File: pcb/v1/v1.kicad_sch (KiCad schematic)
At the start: 0 parts

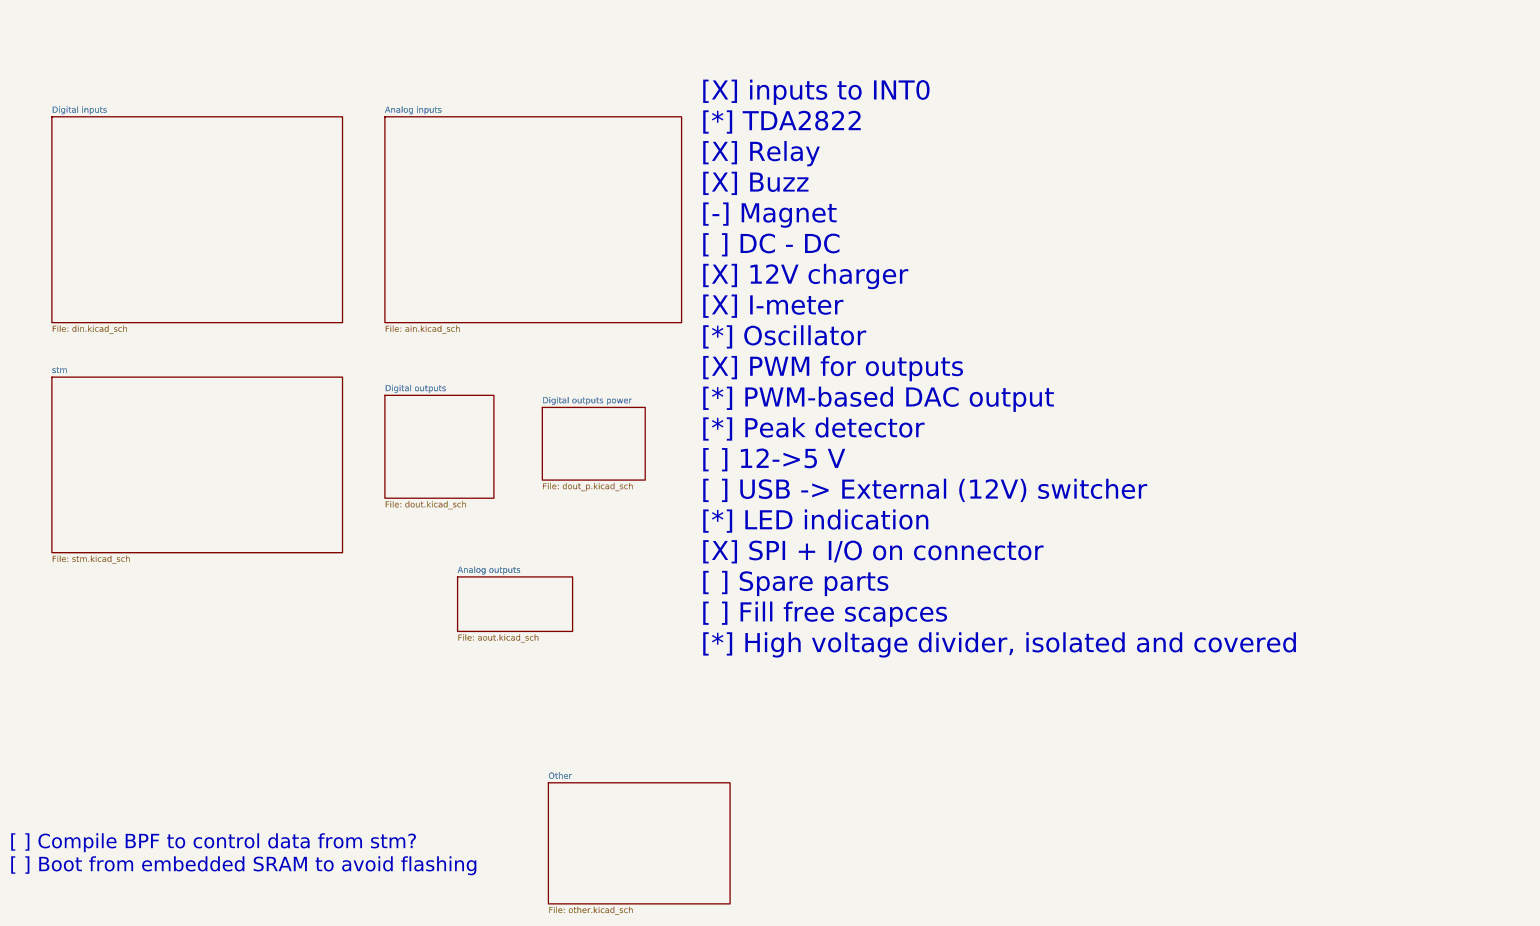
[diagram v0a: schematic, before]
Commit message: Added some spare unused parts and placeholders for future design
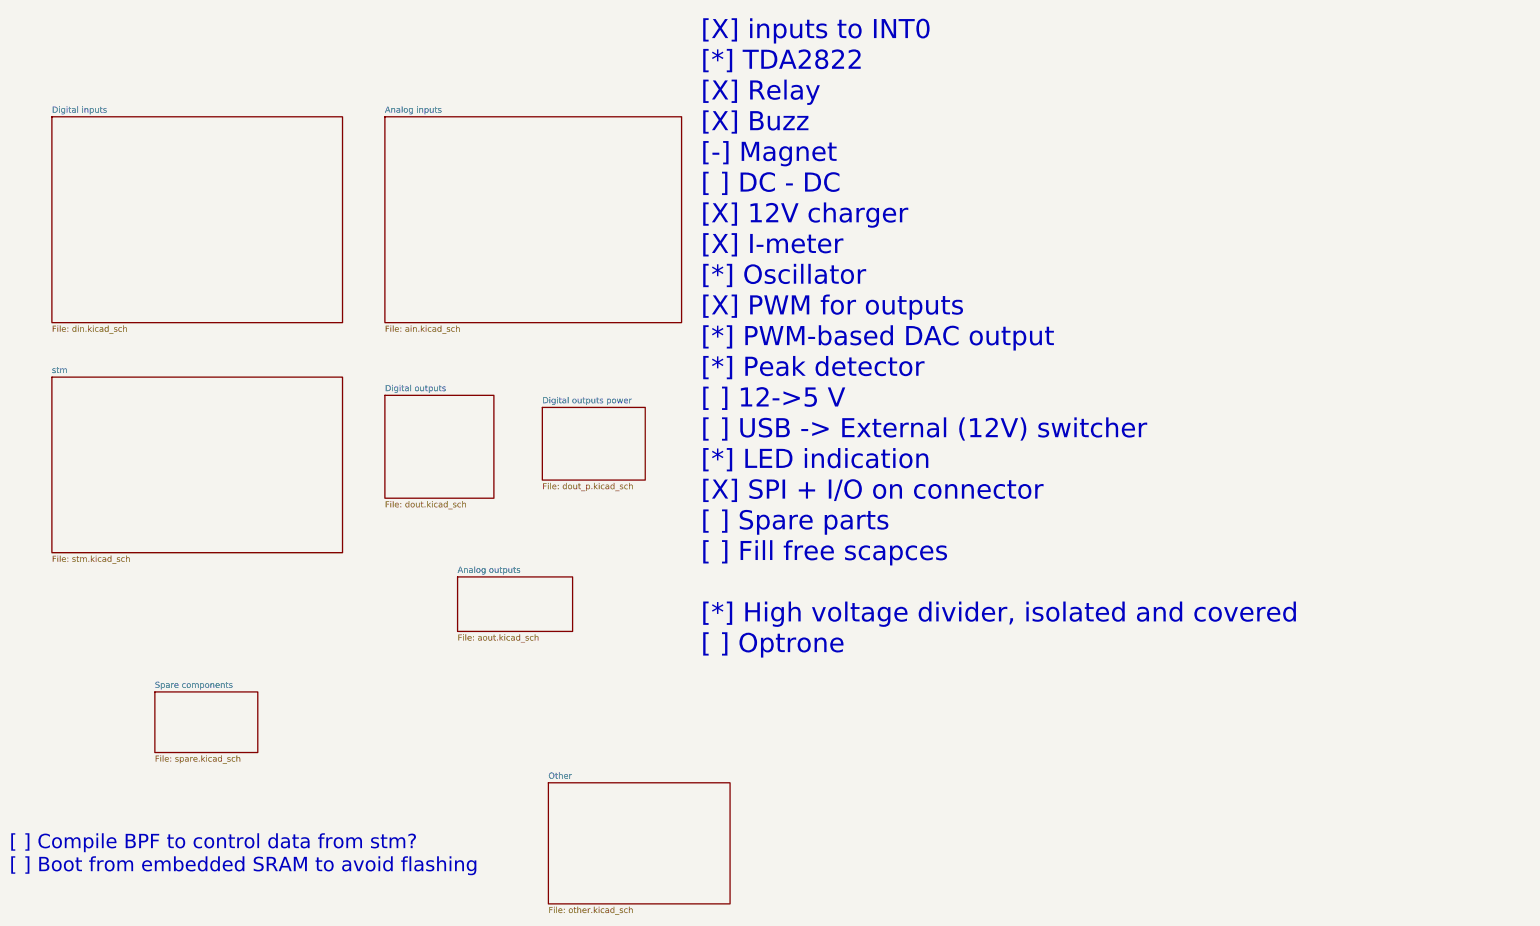
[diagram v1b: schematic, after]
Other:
- added sheet Spare components (spare.kicad_sch)
- note added: "[X] inputs to INT0 [*] TDA2822 [X] Relay [X] Buzz [-] Magnet [ ] DC - DC [X] 12V charger [X] I-meter [*] Oscillator [X] PWM for outputs [*] PWM-based DAC output [*] Peak detector [ ] 12->5 V [ ] USB -> External (12V) switcher [*] LED indication [X] SPI + I/O on connector [ ] Spare parts [ ] Fill free scapces [*] High voltage divider, isolated and covered [ ] Optrone"
- note removed: "[X] inputs to INT0 [*] TDA2822 [X] Relay [X] Buzz [-] Magnet [ ] DC - DC [X] 12V charger [X] I-meter [*] Oscillator [X] PWM for outputs [*] PWM-based DAC output [*] Peak detector [ ] 12->5 V [ ] USB -> External (12V) switcher [*] LED indication [X] SPI + I/O on connector [ ] Spare parts [ ] Fill free scapces [*] High voltage divider, isolated and covered"
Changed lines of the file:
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@@
 	(generator_version "9.0")
 	(paper "A4")
-	(text "[X] inputs to INT0\n[*] TDA2822\n[X] Relay\n[X] Buzz\n[-] Magnet\n[ ] DC - DC\n[X] 12V charger \n[X] I-meter\n[*] Oscillator\n[X] PWM for outputs\n[*] PWM-based DAC output\n[*] Peak detector\n[ ] 12->5 V\n[ ] USB -> External (12V) switcher\n[*] LED indication\n[X] SPI + I/O on connector\n[ ] Spare parts\n[ ] Fill free scapces\n[*] High voltage divider, isolated and covered "
+	(text "[X] inputs to INT0\n[*] TDA2822\n[X] Relay\n[X] Buzz\n[-] Magnet\n[ ] DC - DC\n[X] 12V charger \n[X] I-meter\n[*] Oscillator\n[X] PWM for outputs\n[*] PWM-based DAC output\n[*] Peak detector\n[ ] 12->5 V\n[ ] USB -> External (12V) switcher\n[*] LED indication\n[X] SPI + I/O on connector\n[ ] Spare parts\n[ ] Fill free scapces\n\n[*] High voltage divider, isolated and covered \n[ ] Optrone"
 		(exclude_from_sim no)
 		(at 164.084 142.24 0)
@@
 				)
 			)
+		)
+	)
+	(sheet
+		(at 49.53 149.86)
+		(size 21.59 12.7)
+		(exclude_from_sim no)
+		(in_bom yes)
+		(on_board yes)
+		(dnp no)
+		(fields_autoplaced yes)
+		(stroke
+			(width 0.1524)
+			(type solid)
+		)
+		(fill
+			(color 0 0 0 0.0000)
+		)
+		(property "Sheetname" "Spare components"
+			(at 49.53 149.1484 0)
+			(effects
+				(font
+					(size 1.27 1.27)
+				)
+				(justify left bottom)
+			)
+		)
+		(property "Sheetfile" "spare.kicad_sch"
+			(at 49.53 163.1446 0)
+			(effects
+				(font
+					(size 1.27 1.27)
+				)
+				(justify left top)
+			)
+		)
+		(instances
+			(project "v1"
+				(path "/c9a089ab-5af5-42df-87be-f1df643a1407"
+					(page "9")
+				)
+			)
